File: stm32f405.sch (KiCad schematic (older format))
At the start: 19 parts, among them Q6 CRYSTAL_50X32, U1 STM32F405R

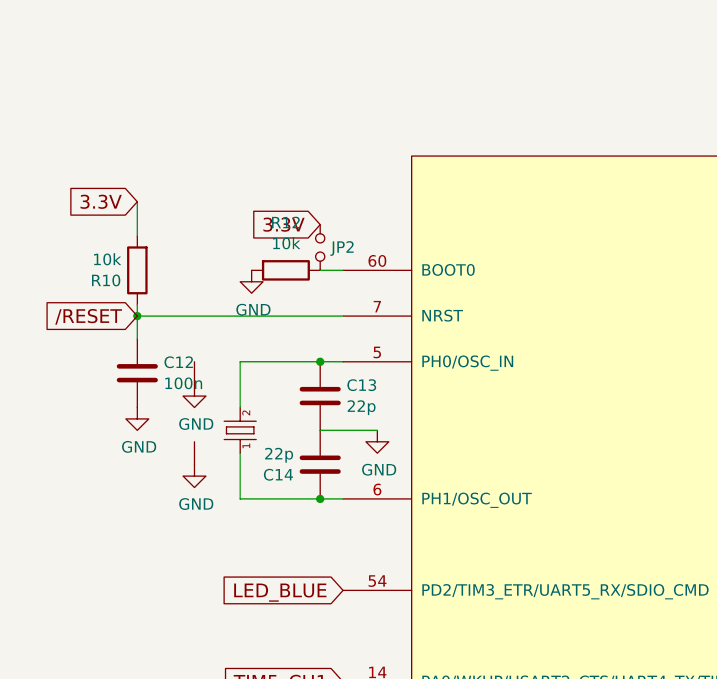
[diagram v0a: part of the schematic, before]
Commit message: routing finished - essential signals only
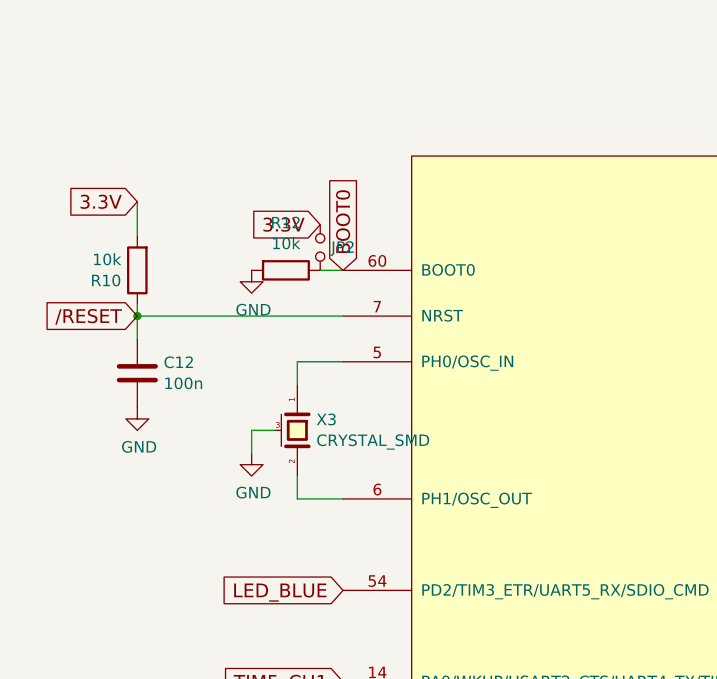
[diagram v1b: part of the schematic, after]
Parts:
- removed C13, C14: 22p, Capacitors_SMD:C_0603, symbol C
- removed Q6: CRYSTAL_50X32, minimal:CRYSTAL_50X32, symbol CRYSTAL_50X32
- added X3: CRYSTAL_SMD, alis_parts:Resonator_3.2x1.3mm, symbol CRYSTAL_SMD
- C10, C11, C12, C6, C7, C8, C9: footprint Capacitors_SMD:C_0603 -> Capacitors_SMD:C_0402
- C5: footprint Capacitors_SMD:C_0805 -> Capacitors_SMD:C_0603
- R10, R12, R16, R17: footprint Resistors_SMD:R_0603 -> Resistors_SMD:R_0402
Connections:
- net GND: now also X3.3 (case)
- net at U1.6 (PH1/OSC_OUT): now also X3.2
- net at U1.5 (PH0/OSC_IN): now also X3.1
- net BOOT0: now reaches JP2.2, R12.1, U1.60 (BOOT0)
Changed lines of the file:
@@
 $Descr A4 11693 8268
 encoding utf-8
-Sheet 3 8
+Sheet 3 7
 Title ""
 Date ""
@@
 F 0 "C6" H 7415 946 50  0000 L CNN
 F 1 "100n" H 7415 854 50  0000 L CNN
-F 2 "Capacitors_SMD:C_0603" H 7338 750 50  0001 C CNN
+F 2 "Capacitors_SMD:C_0402" H 7338 750 50  0001 C CNN
 F 3 "" H 7300 900 50  0000 C CNN
 	1    7300 900
@@
 F 0 "C7" H 7815 946 50  0000 L CNN
 F 1 "100n" H 7815 854 50  0000 L CNN
-F 2 "Capacitors_SMD:C_0603" H 7738 750 50  0001 C CNN
+F 2 "Capacitors_SMD:C_0402" H 7738 750 50  0001 C CNN
 F 3 "" H 7700 900 50  0000 C CNN
 	1    7700 900
@@
 F 0 "C8" H 8215 946 50  0000 L CNN
 F 1 "100n" H 8215 854 50  0000 L CNN
-F 2 "Capacitors_SMD:C_0603" H 8138 750 50  0001 C CNN
+F 2 "Capacitors_SMD:C_0402" H 8138 750 50  0001 C CNN
 F 3 "" H 8100 900 50  0000 C CNN
 	1    8100 900
@@
 F 0 "C9" H 8615 946 50  0000 L CNN
 F 1 "100n" H 8615 854 50  0000 L CNN
-F 2 "Capacitors_SMD:C_0603" H 8538 750 50  0001 C CNN
+F 2 "Capacitors_SMD:C_0402" H 8538 750 50  0001 C CNN
 F 3 "" H 8500 900 50  0000 C CNN
 	1    8500 900
@@
 F 0 "C5" H 7015 946 50  0000 L CNN
 F 1 "4.7u" H 7015 854 50  0000 L CNN
-F 2 "Capacitors_SMD:C_0805" H 6938 750 50  0001 C CNN
+F 2 "Capacitors_SMD:C_0603" H 6938 750 50  0001 C CNN
 F 3 "" H 6900 900 50  0000 C CNN
 	1    6900 900
@@
 $EndComp
 $Comp
-L GND #PWR010
+L GND #PWR06
 U 1 1 569AE259
 P 5550 7400
-F 0 "#PWR010" H 5550 7150 50  0001 C CNN
+F 0 "#PWR06" H 5550 7150 50  0001 C CNN
 F 1 "GND" H 5558 7226 50  0000 C CNN
 F 2 "" H 5550 7400 50  0000 C CNN
@@
 F 0 "C11" H 4515 1346 50  0000 L CNN
 F 1 "100n" H 4515 1254 50  0000 L CNN
-F 2 "Capacitors_SMD:C_0603" H 4438 1150 50  0001 C CNN
+F 2 "Capacitors_SMD:C_0402" H 4438 1150 50  0001 C CNN
 F 3 "" H 4400 1300 50  0000 C CNN
 	1    4400 1300
@@
 F 0 "C10" H 4115 1346 50  0000 L CNN
 F 1 "1u" H 4115 1254 50  0000 L CNN
-F 2 "Capacitors_SMD:C_0603" H 4038 1150 50  0001 C CNN
+F 2 "Capacitors_SMD:C_0402" H 4038 1150 50  0001 C CNN
 F 3 "" H 4000 1300 50  0000 C CNN
 	1    4000 1300
@@
 $EndComp
 $Comp
-L GND #PWR011
+L GND #PWR07
 U 1 1 569AE27B
 P 4000 1650
-F 0 "#PWR011" H 4000 1400 50  0001 C CNN
+F 0 "#PWR07" H 4000 1400 50  0001 C CNN
 F 1 "GND" H 4008 1476 50  0000 C CNN
 F 2 "" H 4000 1650 50  0000 C CNN
@@
 F 0 "R10" H 1220 2446 50  0000 L CNN
 F 1 "10k" H 1220 2354 50  0000 L CNN
-F 2 "Resistors_SMD:R_0603" V 1080 2400 50  0001 C CNN
+F 2 "Resistors_SMD:R_0402" V 1080 2400 50  0001 C CNN
 F 3 "" H 1150 2400 50  0000 C CNN
 	1    1150 2400
@@
 F 0 "C12" H 1265 2896 50  0000 L CNN
 F 1 "100n" H 1265 2804 50  0000 L CNN
-F 2 "Capacitors_SMD:C_0603" H 1188 2700 50  0001 C CNN
+F 2 "Capacitors_SMD:C_0402" H 1188 2700 50  0001 C CNN
 F 3 "" H 1150 2850 50  0000 C CNN
 	1    1150 2850
@@
 $EndComp
 $Comp
-L GND #PWR012
+L GND #PWR08
 U 1 1 569AE29F
 P 1150 3000
-F 0 "#PWR012" H 1150 2750 50  0001 C CNN
+F 0 "#PWR08" H 1150 2750 50  0001 C CNN
 F 1 "GND" H 1158 2826 50  0000 C CNN
 F 2 "" H 1150 3000 50  0000 C CNN
@@
 $EndComp
 $Comp
-L CRYSTAL_50X32 Q?
-U 3 1 569AE2A5
-P 1600 3100
-AR Path="/569AE2A5" Ref="Q?"  Part="3"
-AR Path="/56980F8D/569AE2A5" Ref="Q6"  Part="3"
-F 0 "Q6" H 1600 3100 50  0001 C CNN
-F 1 "CRYSTAL_50X32" H 1600 3100 50  0001 C CNN
-F 2 "minimal:CRYSTAL_50X32" H 1630 3250 20  0001 C CNN
-F 3 "" H 1600 3100 60  0000 C CNN
-	3    1600 3100
-	0    -1   -1   0
-$EndComp
-$Comp
-L CRYSTAL_50X32 Q?
-U 2 1 569AE2AB
-P 1400 2800
-AR Path="/569AE2AB" Ref="Q?"  Part="2"
-AR Path="/56980F8D/569AE2AB" Ref="Q6"  Part="2"
-F 0 "Q6" H 1400 2800 50  0001 C CNN
-F 1 "CRYSTAL_50X32" H 1400 2800 50  0001 C CNN
-F 2 "minimal:CRYSTAL_50X32" H 1430 2950 20  0001 C CNN
-F 3 "" H 1400 2800 60  0000 C CNN
-	2    1400 2800
-	1    0    0    -1
-$EndComp
-$Comp
-L CRYSTAL_50X32 Q?
-U 1 1 569AE2B1
-P 1400 3150
-AR Path="/569AE2B1" Ref="Q?"  Part="1"
-AR Path="/56980F8D/569AE2B1" Ref="Q6"  Part="1"
-F 0 "Q6" H 1400 3150 50  0001 C CNN
-F 1 "CRYSTAL_50X32" H 1400 3150 50  0001 C CNN
-F 2 "minimal:CRYSTAL_50X32" H 1430 3300 20  0001 C CNN
-F 3 "" H 1400 3150 60  0000 C CNN
-	1    1400 3150
-	1    0    0    -1
-$EndComp
-$Comp
-L GND #PWR013
-U 1 1 569AE2B7
-P 1400 2900
-F 0 "#PWR013" H 1400 2650 50  0001 C CNN
-F 1 "GND" H 1408 2726 50  0000 C CNN
-F 2 "" H 1400 2900 50  0000 C CNN
-F 3 "" H 1400 2900 50  0000 C CNN
-	1    1400 2900
-	1    0    0    -1
-$EndComp
-$Comp
-L GND #PWR014
-U 1 1 569AE2BD
-P 1400 3250
-F 0 "#PWR014" H 1400 3000 50  0001 C CNN
-F 1 "GND" H 1408 3076 50  0000 C CNN
-F 2 "" H 1400 3250 50  0000 C CNN
-F 3 "" H 1400 3250 50  0000 C CNN
-	1    1400 3250
-	1    0    0    -1
-$EndComp
-$Comp
-L C C13
-U 1 1 569AE2C3
-P 1950 2950
-F 0 "C13" H 2065 2996 50  0000 L CNN
-F 1 "22p" H 2065 2904 50  0000 L CNN
-F 2 "Capacitors_SMD:C_0603" H 1988 2800 50  0001 C CNN
-F 3 "" H 1950 2950 50  0000 C CNN
-	1    1950 2950
-	1    0    0    -1
-$EndComp
-$Comp
-L C C14
-U 1 1 569AE2CA
-P 1950 3250
-F 0 "C14" H 2065 3296 50  0000 L CNN
-F 1 "22p" H 2065 3204 50  0000 L CNN
-F 2 "Capacitors_SMD:C_0603" H 1988 3100 50  0001 C CNN
-F 3 "" H 1950 3250 50  0000 C CNN
-	1    1950 3250
-	-1   0    0    1
-$EndComp
-$Comp
-L GND #PWR015
+L GND #PWR09
 U 1 1 569AE2D1
-P 2200 3100
-F 0 "#PWR015" H 2200 2850 50  0001 C CNN
-F 1 "GND" H 2208 2926 50  0000 C CNN
-F 2 "" H 2200 3100 50  0000 C CNN
-F 3 "" H 2200 3100 50  0000 C CNN
-	1    2200 3100
+P 1650 3200
+F 0 "#PWR09" H 1650 2950 50  0001 C CNN
+F 1 "GND" H 1658 3026 50  0000 C CNN
+F 2 "" H 1650 3200 50  0000 C CNN
+F 3 "" H 1650 3200 50  0000 C CNN
+	1    1650 3200
 	1    0    0    -1
 $EndComp
@@
 	1    0    0    -1
 $EndComp
-Wire Wire Line
-	2200 3100 1950 3100
-Connection ~ 1950 3400
-Wire Wire Line
-	1600 3400 2050 3400
-Wire Wire Line
-	1600 3200 1600 3400
-Connection ~ 1950 2800
-Wire Wire Line
-	1600 2800 1600 3000
-Wire Wire Line
-	1600 2800 2050 2800
 Connection ~ 1150 2600
 Wire Wire Line
@@
 	4000 750  8500 750
 $Comp
-L GND #PWR016
+L GND #PWR010
 U 1 1 569E1F9F
 P 1650 2400
-F 0 "#PWR016" H 1650 2150 50  0001 C CNN
+F 0 "#PWR010" H 1650 2150 50  0001 C CNN
 F 1 "GND" H 1658 2226 50  0000 C CNN
 F 2 "" H 1650 2400 50  0000 C CNN
@@
 Connection ~ 6900 750
 $Comp
-L GND #PWR017
+L GND #PWR011
 U 1 1 569E5F3D
 P 8500 1250
-F 0 "#PWR017" H 8500 1000 50  0001 C CNN
+F 0 "#PWR011" H 8500 1000 50  0001 C CNN
 F 1 "GND" H 8508 1076 50  0000 C CNN
 F 2 "" H 8500 1250 50  0000 C CNN
@@
 F 0 "R12" V 1593 2400 50  0000 C CNN
 F 1 "10k" V 1684 2400 50  0000 C CNN
-F 2 "Resistors_SMD:R_0603" V 1730 2400 50  0001 C CNN
+F 2 "Resistors_SMD:R_0402" V 1730 2400 50  0001 C CNN
 F 3 "" H 1800 2400 50  0000 C CNN
 	1    1800 2400
@@
 F 0 "R17" H 10870 2846 50  0000 L CNN
 F 1 "22k" H 10870 2754 50  0000 L CNN
-F 2 "Resistors_SMD:R_0603" V 10730 2800 50  0001 C CNN
+F 2 "Resistors_SMD:R_0402" V 10730 2800 50  0001 C CNN
 F 3 "" H 10800 2800 50  0000 C CNN
 	1    10800 2800
@@
 F 0 "R16" H 10670 2846 50  0000 L CNN
 F 1 "22k" H 10670 2754 50  0000 L CNN
-F 2 "Resistors_SMD:R_0603" V 10530 2800 50  0001 C CNN
+F 2 "Resistors_SMD:R_0402" V 10530 2800 50  0001 C CNN
 F 3 "" H 10600 2800 50  0000 C CNN
 	1    10600 2800
@@
 Text GLabel 10800 2650 1    60   Input ~ 0
 3.3V
+$Comp
+L CRYSTAL_SMD X3
+U 1 1 57535D05
+P 1850 3100
+F 0 "X3" V 1804 3183 50  0000 L CNN
+F 1 "CRYSTAL_SMD" V 1895 3183 50  0000 L CNN
+F 2 "alis_parts:Resonator_3.2x1.3mm" H 1850 3100 50  0001 C CNN
+F 3 "" H 1850 3100 50  0000 C CNN
+	1    1850 3100
+	0    1    1    0
+$EndComp
+Wire Wire Line
+	1850 3300 1850 3400
+Wire Wire Line
+	1850 3400 2050 3400
+Wire Wire Line
+	1850 2900 1850 2800
+Wire Wire Line
+	1850 2800 2050 2800
+Wire Wire Line
+	1650 3200 1650 3100
+Wire Wire Line
+	1650 3100 1750 3100
+Text GLabel 2050 2400 1    60   Input ~ 0
+BOOT0
 $EndSCHEMATC
